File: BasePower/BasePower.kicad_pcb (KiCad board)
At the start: 4 copper layers, 80.5 x 40 mm, 59 parts, among them J1 VIN, J2 3.3V, U1 TPS552892, U2 TLVM13640, U3 TPSM33625F

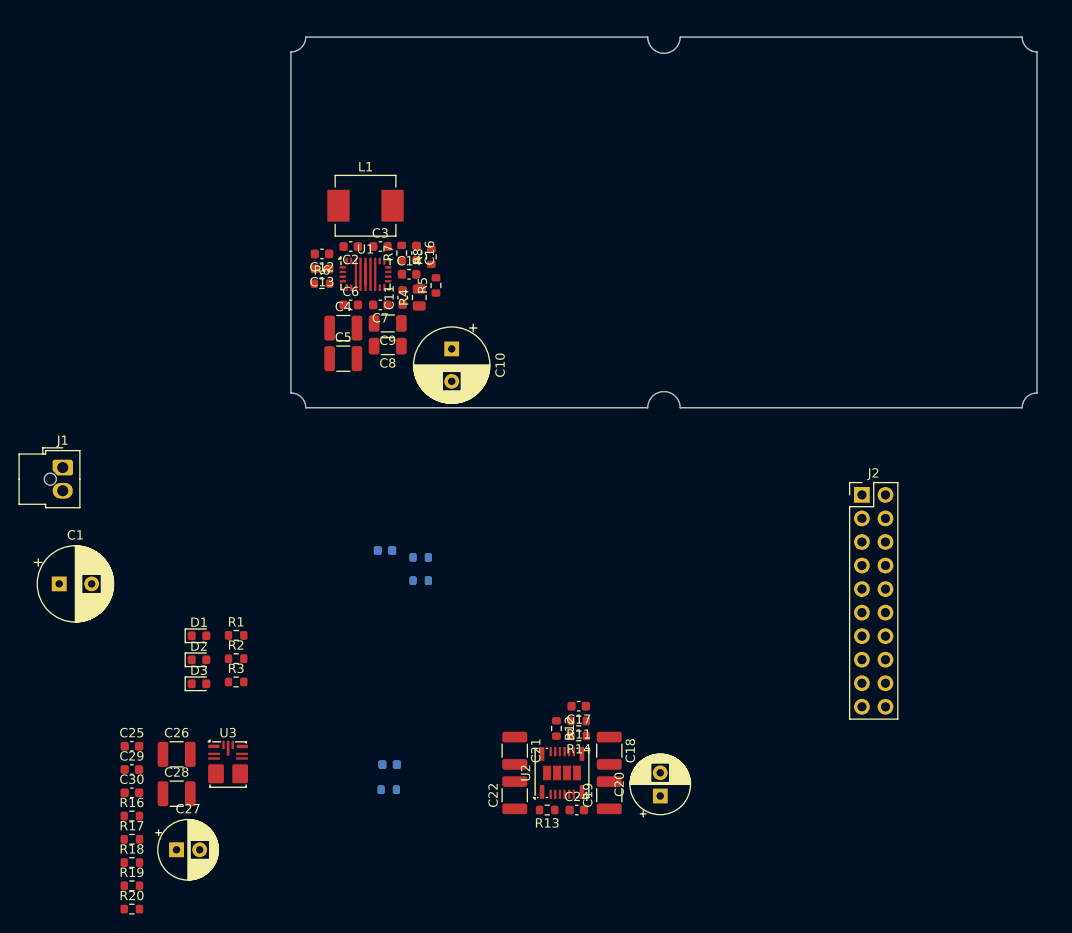
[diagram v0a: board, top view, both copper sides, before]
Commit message: BasePower layout mostly done
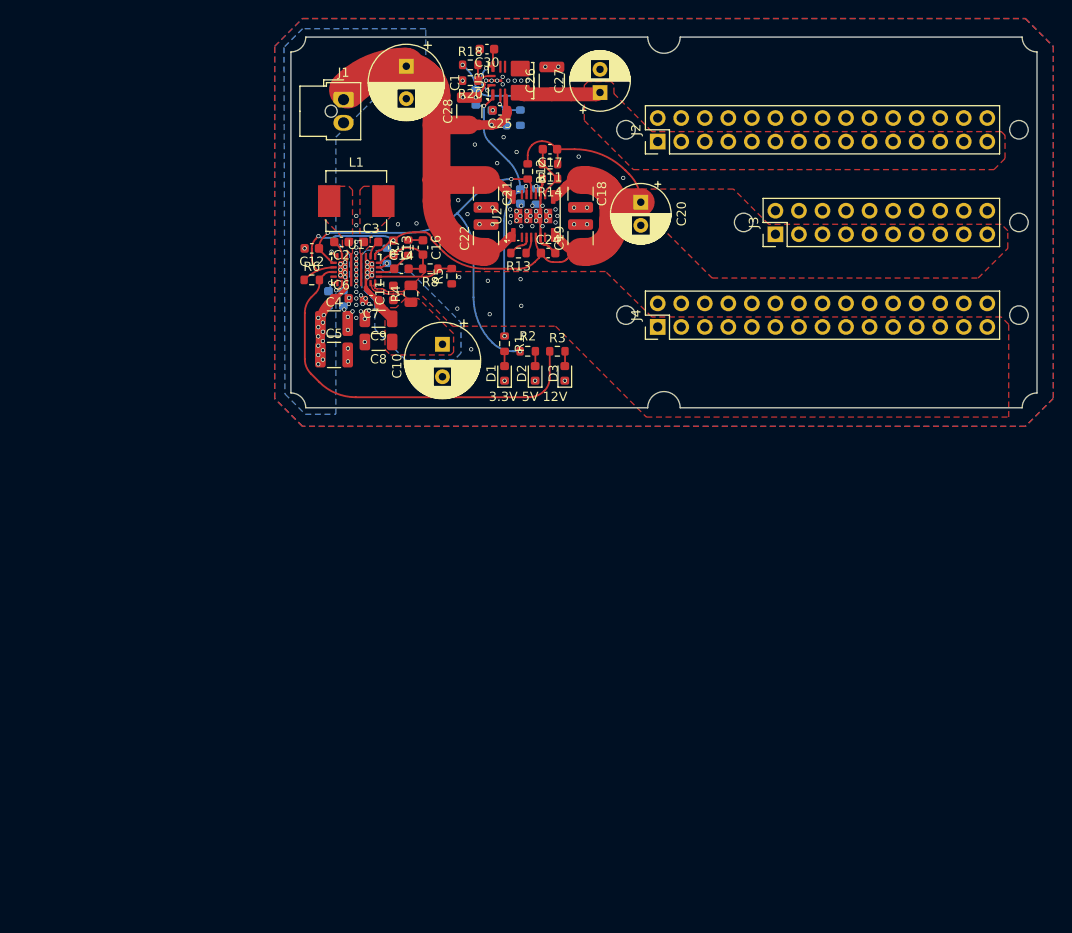
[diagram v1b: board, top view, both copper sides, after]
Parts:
- added Hole1: Hole_2mm, BW_PassiveMechanical:Hole_2mm, F.Cu at (145.9, 90.0)
- added Hole2: Hole_2mm, BW_PassiveMechanical:Hole_2mm, F.Cu at (188.3, 90.0)
- added Hole3: Hole_2mm, BW_PassiveMechanical:Hole_2mm, F.Cu at (158.6, 100.0)
- added Hole4: Hole_2mm, BW_PassiveMechanical:Hole_2mm, F.Cu at (188.3, 100.0)
- added Hole5: Hole_2mm, BW_PassiveMechanical:Hole_2mm, F.Cu at (145.9, 110.0)
- added Hole6: Hole_2mm, BW_PassiveMechanical:Hole_2mm, F.Cu at (188.3, 110.0)
- added J3: 5V, Connector_PinHeader_2.54mm:PinHeader_2x10_P2.54mm_Vertical, F.Cu at (162.0, 101.3)
- added J4: 12V, Connector_PinHeader_2.54mm:PinHeader_2x15_P2.54mm_Vertical, F.Cu at (149.3, 111.3)
- C29, R16, R17, R19: moved to B.Cu
- J2: footprint Connector_PinHeader_2.54mm:PinHeader_2x10_P2.54mm_Vertical -> Connector_PinHeader_2.54mm:PinHeader_2x15_P2.54mm_Vertical
- moved R20 96.6 mm to (129.1, 84.7), turned to 180 degrees
- moved C27 93.6 mm to (143.1, 86.0), turned to 90 degrees
- moved R18 93.5 mm to (129.1, 83.0)
- moved R19 92.9 mm to (134.5, 88.7), turned to -90 degrees
- moved C30 88.9 mm to (130.9, 81.3), turned to 180 degrees
- moved R17 88.2 mm to (129.7, 86.5), turned to -90 degrees
- moved R16 84.4 mm to (132.2, 89.5)
- moved C26 83.2 mm to (137.9, 84.7), turned to 90 degrees
- moved C29 81.4 mm to (132.2, 87.9), turned to 180 degrees
- moved C28 80.1 mm to (129.0, 88.0), turned to 90 degrees
- moved U3 79.9 mm to (133.5, 84.7), turned to 90 degrees
- moved C25 79.3 mm to (132.3, 87.9), turned to 180 degrees
- moved C1 67.2 mm to (122.2, 83.1), turned to -90 degrees
- moved R15 65.9 mm to (136.2, 97.2), turned to -90 degrees
- moved C20 64.1 mm to (147.5, 97.8), turned to -90 degrees
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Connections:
- J2 pad 1: GND -> /3.3V Buck/3.3V
- J2 pad 10: /3.3V Buck/3.3V -> GND
- J2 pad 11: GND -> /3.3V Buck/3.3V
- J2 pad 12: /3.3V Buck/3.3V -> GND
- J2 pad 13: GND -> /3.3V Buck/3.3V
- J2 pad 14: /3.3V Buck/3.3V -> GND
- J2 pad 15: GND -> /3.3V Buck/3.3V
- J2 pad 16: /3.3V Buck/3.3V -> GND
- J2 pad 17: GND -> /3.3V Buck/3.3V
- J2 pad 18: /3.3V Buck/3.3V -> GND
- J2 pad 19: GND -> /3.3V Buck/3.3V
- J2 pad 2: /3.3V Buck/3.3V -> GND
- J2 pad 20: /3.3V Buck/3.3V -> GND
- J2 pad 3: GND -> /3.3V Buck/3.3V
- J2 pad 4: /3.3V Buck/3.3V -> GND
- J2 pad 5: GND -> /3.3V Buck/3.3V
- J2 pad 6: /3.3V Buck/3.3V -> GND
- J2 pad 7: GND -> /3.3V Buck/3.3V
- J2 pad 8: /3.3V Buck/3.3V -> GND
- J2 pad 9: GND -> /3.3V Buck/3.3V
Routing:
- net /12V Buck-Boost/5V: track 0.00 -> 85.0 mm, vias 0 -> 2
- net /12V Buck-Boost/VIN: track 0.00 -> 66.0 mm, vias 0 -> 20
- net /5V Buck/5VPG: track 0.00 -> 47.5 mm, vias 0 -> 3
- net /12V Buck-Boost/PG: track 0.00 -> 43.2 mm
- net /3.3V Buck/PG: track 0.00 -> 30.8 mm, vias 0 -> 3
- net /3.3V Buck/3.3V: track 0.00 -> 25.5 mm, vias 0 -> 1
- net GND: track 0.00 -> 22.1 mm, vias 0 -> 104
- net Net-(U1-ISP): track 0.00 -> 12.4 mm, vias 0 -> 7
- net Net-(U1-FB): track 0.00 -> 8.22 mm
- net Net-(U3-RT/MODE/SYNC): track 0.00 -> 6.24 mm, vias 0 -> 2
- net Net-(U2-FB): track 0.00 -> 6.14 mm
- net /12V Buck-Boost/12V: track 0.00 -> 5.45 mm
- net Net-(U3-EN): track 0.00 -> 5.18 mm, vias 0 -> 1
- net Net-(U1-COMP): track 0.00 -> 3.83 mm
- net Net-(U3-FB/BIAS): track 0.00 -> 3.29 mm
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- added copper zone on F.Cu, net /12V Buck-Boost/12V
- added copper zone on F.Cu, net /12V Buck-Boost/5V
- added copper zone on B.Cu, net /12V Buck-Boost/VIN
- added copper zone on F.Cu, net /3.3V Buck/3.3V
- added copper zone on B.Cu, net GND
- added copper zone on F.Cu, net GND
- added copper zone on In1.Cu, net GND
- added copper zone on In2.Cu, net GND
- added copper zone on B.Cu, net Net-(U1-ISP)
- added copper zone on F.Cu, net Net-(U1-ISP)
- added copper zone on F.Cu, net Net-(U1-SW1)
- added copper zone on F.Cu, net Net-(U1-SW2)
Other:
- board text added: "3.3V 5V 12V"

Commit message: BasePower design and inventory done
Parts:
- added C2: ?pF, Capacitor_SMD:C_0603_1608Metric, F.Cu at (111.5, 98.5)
- added C3: ?pF, Capacitor_SMD:C_0603_1608Metric, F.Cu at (122.1, 98.5)
- added R4: ?Ω, Resistor_SMD:R_1206_3216Metric, F.Cu at (111.1, 94.6)
- added R5: ?Ω, Resistor_SMD:R_1206_3216Metric, F.Cu at (122.5, 94.6)
- added R6: 50Ω, Resistor_SMD:R_0603_1608Metric, B.Cu at (116.0, 97.1)
- added R7: 50Ω, Resistor_SMD:R_0603_1608Metric, B.Cu at (122.2, 95.0)
- added REF**: BW_Logo_7.5x4.8mm, BW_Logo:BW_Logo_7.5x4.8mm, F.Cu at (182.1, 83.6)
- added TP1: SW1, Connector_Coaxial:U.FL_Molex_MCRF_73412-0110_Vertical, B.Cu at (116.8, 93.7)
- added TP2: SW2, Connector_Coaxial:U.FL_Molex_MCRF_73412-0110_Vertical, B.Cu at (123.2, 98.4)
- renumbered C8 to C10, C9 to C11, C10 to C12, C11 to C13, C12 to C14, C13 to C15, C14 to C16, C15 to C17, C16 to C18, C17 to C19, C18 to C20, C19 to C21, C20 to C22, C21 to C23, C22 to C24, C23 to C25, C24 to C26, C25 to C27, C26 to C28, C27 to C29, C28 to C30, C29 to C31, C30 to C32, C2 to C4, C3 to C5, C4 to C6, C5 to C7, C6 to C8, C7 to C9, R6 to R10, R7 to R11, R8 to R12, R9 to R13, R10 to R14, R11 to R15, R12 to R16, R13 to R17, R14 to R18, R15 to R19, R16 to R20, R17 to R21, R18 to R22, R19 to R23, R20 to R24, R4 to R8, R5 to R9
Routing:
- net GND: track 22.1 -> 35.4 mm, vias 104 -> 108
- net Net-(U1-SW2): track 0.00 -> 5.01 mm, vias 0 -> 1
- net Net-(U1-SW1): track 0.00 -> 3.08 mm, vias 0 -> 1
- net Net-(TP2-In): track 0.00 -> 1.94 mm
- net Net-(TP1-In): track 0.00 -> 1.91 mm
- net Net-(C2-Pad1): track 0.00 -> 1.76 mm
- net Net-(C3-Pad1): track 0.00 -> 1.76 mm
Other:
- board text added: "+ -"
- board text added: "12V"
- board text added: "3.3V"
- board text added: "5V"
- board text added: "Modular Audio Base Power"
- board text added: "Power Good"

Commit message: BasePower v1.1: Now with fuses
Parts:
- added F1: 2.5A, Fuse:Fuse_0603_1608Metric, F.Cu at (145.9, 92.8)
- added F2: 4A, Fuse:Fuse_0603_1608Metric, F.Cu at (152.5, 97.8)
- added F3: 5A, Fuse:Fuse_0603_1608Metric, F.Cu at (127.8, 108.2)
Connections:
- J2 pad 1: /3.3V Buck/3.3V -> Net-(J2-Pin_1)
- J2 pad 11: /3.3V Buck/3.3V -> Net-(J2-Pin_1)
- J2 pad 13: /3.3V Buck/3.3V -> Net-(J2-Pin_1)
- J2 pad 15: /3.3V Buck/3.3V -> Net-(J2-Pin_1)
- J2 pad 17: /3.3V Buck/3.3V -> Net-(J2-Pin_1)
- J2 pad 19: /3.3V Buck/3.3V -> Net-(J2-Pin_1)
- J2 pad 21: /3.3V Buck/3.3V -> Net-(J2-Pin_1)
- J2 pad 23: /3.3V Buck/3.3V -> Net-(J2-Pin_1)
- J2 pad 25: /3.3V Buck/3.3V -> Net-(J2-Pin_1)
- J2 pad 27: /3.3V Buck/3.3V -> Net-(J2-Pin_1)
- J2 pad 29: /3.3V Buck/3.3V -> Net-(J2-Pin_1)
- J2 pad 3: /3.3V Buck/3.3V -> Net-(J2-Pin_1)
- J2 pad 5: /3.3V Buck/3.3V -> Net-(J2-Pin_1)
- J2 pad 7: /3.3V Buck/3.3V -> Net-(J2-Pin_1)
- J2 pad 9: /3.3V Buck/3.3V -> Net-(J2-Pin_1)
- J3 pad 1: /12V Buck-Boost/5V -> Net-(J3-Pin_1)
- J3 pad 11: /12V Buck-Boost/5V -> Net-(J3-Pin_1)
- J3 pad 13: /12V Buck-Boost/5V -> Net-(J3-Pin_1)
- J3 pad 15: /12V Buck-Boost/5V -> Net-(J3-Pin_1)
- J3 pad 17: /12V Buck-Boost/5V -> Net-(J3-Pin_1)
- J3 pad 19: /12V Buck-Boost/5V -> Net-(J3-Pin_1)
- J3 pad 3: /12V Buck-Boost/5V -> Net-(J3-Pin_1)
- J3 pad 5: /12V Buck-Boost/5V -> Net-(J3-Pin_1)
- J3 pad 7: /12V Buck-Boost/5V -> Net-(J3-Pin_1)
- J3 pad 9: /12V Buck-Boost/5V -> Net-(J3-Pin_1)
- J4 pad 1: /12V Buck-Boost/12V -> Net-(J4-Pin_1)
- J4 pad 11: /12V Buck-Boost/12V -> Net-(J4-Pin_1)
- J4 pad 13: /12V Buck-Boost/12V -> Net-(J4-Pin_1)
- J4 pad 15: /12V Buck-Boost/12V -> Net-(J4-Pin_1)
- J4 pad 17: /12V Buck-Boost/12V -> Net-(J4-Pin_1)
- J4 pad 19: /12V Buck-Boost/12V -> Net-(J4-Pin_1)
- J4 pad 21: /12V Buck-Boost/12V -> Net-(J4-Pin_1)
- J4 pad 23: /12V Buck-Boost/12V -> Net-(J4-Pin_1)
- J4 pad 25: /12V Buck-Boost/12V -> Net-(J4-Pin_1)
- J4 pad 27: /12V Buck-Boost/12V -> Net-(J4-Pin_1)
- J4 pad 29: /12V Buck-Boost/12V -> Net-(J4-Pin_1)
- J4 pad 3: /12V Buck-Boost/12V -> Net-(J4-Pin_1)
- J4 pad 5: /12V Buck-Boost/12V -> Net-(J4-Pin_1)
- J4 pad 7: /12V Buck-Boost/12V -> Net-(J4-Pin_1)
- J4 pad 9: /12V Buck-Boost/12V -> Net-(J4-Pin_1)
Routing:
- net /3.3V Buck/3.3V: track 25.5 -> 32.4 mm
- net /12V Buck-Boost/5V: track 85.0 -> 89.3 mm
- added copper zone on F.Cu, net Net-(J2-Pin_1)
- added copper zone on F.Cu, net Net-(J3-Pin_1)
- added copper zone on F.Cu, net Net-(J4-Pin_1)
- removed copper zone on F.Cu, net /12V Buck-Boost/5V
- removed copper zone on F.Cu, net /3.3V Buck/3.3V
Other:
- board text added: "2.5A max"
- board text added: "4A max"
- board text added: "5A max"
- board text added: "Modular Audio Base Power v1.1"
- board text removed: "Modular Audio Base Power"

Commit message: BasePower v1.2 + inventory
Added 12V clean LDO and improved power good display
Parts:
- removed the R10 at (112.0, 106.2)
- removed the R16 at (135.3, 94.5)
- removed the R21 at (129.7, 86.5)
- added C33: 10µF 50V, Capacitor_SMD:C_1206_3216Metric, B.Cu at (141.8, 107.5)
- added C34: 0.1µF, Capacitor_SMD:C_0603_1608Metric, B.Cu at (141.0, 109.4)
- added C35: 22µF 16V, Capacitor_SMD:C_1210_3225Metric, B.Cu at (141.8, 112.3)
- added C36: 470µF 16V, Capacitor_THT:CP_Radial_D6.3mm_P2.50mm, F.Cu at (158.9, 116.5)
- added C37: 1µF 50Vl, Capacitor_SMD:C_0805_2012Metric, B.Cu at (136.1, 106.1)
- added D4: Green, LED_SMD:LED_0603_1608Metric, F.Cu at (141.6, 116.3)
- added JP1: 0.8V, Jumper:SolderJumper-2_P1.3mm_Open_RoundedPad1.0x1.5mm, B.Cu at (131.4, 113.6)
- added JP2: 0.2V, Jumper:SolderJumper-2_P1.3mm_Open_RoundedPad1.0x1.5mm, B.Cu at (131.4, 108.4)
- added JP3: 0.4V, Jumper:SolderJumper-2_P1.3mm_Open_RoundedPad1.0x1.5mm, B.Cu at (131.4, 111.0)
- added JP4: 0.1V, Jumper:SolderJumper-2_P1.3mm_Open_RoundedPad1.0x1.5mm, B.Cu at (132.6, 105.8)
- added Q1: NX138BK, Package_TO_SOT_SMD:SOT-23, B.Cu at (138.6, 117.6)
- added Q2: NX138BK, Package_TO_SOT_SMD:SOT-23, B.Cu at (142.6, 117.6)
- added R1: 1kΩ, Resistor_SMD:R_0603_1608Metric, B.Cu at (132.4, 91.8)
- added R3: 3.3kΩ, Resistor_SMD:R_0603_1608Metric, F.Cu at (135.3, 94.3)
- added R5: 2kΩ, Resistor_SMD:R_0603_1608Metric, F.Cu at (111.6, 105.2)
- added R7: 1kΩ, Resistor_SMD:R_0603_1608Metric, F.Cu at (140.1, 114.8)
- added R8: 4.7kΩ, Resistor_SMD:R_0603_1608Metric, B.Cu at (146.9, 115.8)
- added R9: 1kΩ, Resistor_SMD:R_0603_1608Metric, B.Cu at (145.3, 117.6)
- added U4: TPS7A47, Package_DFN_QFN:Texas_RGW0020A_VQFN-20-1EP_5x5mm_P0.65mm_EP3.15x3.15mm, B.Cu at (136.3, 110.4)
- R2: renamed from R1; value ?kΩ -> 0Ω
- R4: renamed from R2; value ?kΩ -> 0Ω
- R6: renamed from R3; value ?kΩ -> 1kΩ
- moved D1 0.80 mm to (132.0, 116.3)
- moved D3 0.80 mm to (138.5, 116.3)
- moved R2 0.80 mm to (132.0, 113.1)
- moved R4 0.80 mm to (134.5, 113.9)
- moved R6 0.80 mm to (137.7, 113.9)
- moved D2 0.80 mm to (135.3, 116.3)
- moved TP2 0.10 mm to (123.2, 98.3)
- renumbered R4 to R10, R5 to R11, R6 to R12, R7 to R13, R8 to R14, R9 to R15, R11 to R16, R12 to R17, R13 to R18, R14 to R19, R15 to R20, R17 to R21, R18 to R22, R19 to R23, R20 to R24, R22 to R25, R23 to R26, R24 to R27
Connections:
- net /5V Buck/5VPG renamed /12V Buck-Boost/EN
- D3 pad 1: GND -> Net-(D3-K)
- F3 pad 2: Net-(J4-Pin_1) -> /12V Clean LDO/12V
- J4 pad 1: Net-(J4-Pin_1) -> /12V Clean LDO/12V
- J4 pad 11: Net-(J4-Pin_1) -> /12V Clean LDO/12V
- J4 pad 13: Net-(J4-Pin_1) -> /12V Clean LDO/12V
- J4 pad 15: Net-(J4-Pin_1) -> /12V Clean LDO/12V
- J4 pad 17: Net-(J4-Pin_1) -> /12V Clean LDO/12V
- J4 pad 19: Net-(J4-Pin_1) -> /12V Clean LDO/12V
- J4 pad 21: Net-(J4-Pin_1) -> /12V Clean LDO/12V
- J4 pad 23: Net-(J4-Pin_1) -> /12V Clean LDO/12V
- J4 pad 25: Net-(J4-Pin_1) -> /12V Clean LDO/12VC
- J4 pad 27: Net-(J4-Pin_1) -> /12V Clean LDO/12VC
- J4 pad 29: Net-(J4-Pin_1) -> /12V Clean LDO/12VC
- J4 pad 3: Net-(J4-Pin_1) -> /12V Clean LDO/12V
- J4 pad 5: Net-(J4-Pin_1) -> /12V Clean LDO/12V
- J4 pad 7: Net-(J4-Pin_1) -> /12V Clean LDO/12V
- J4 pad 9: Net-(J4-Pin_1) -> /12V Clean LDO/12V
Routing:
- net /12V Clean LDO/12VC: track 0.00 -> 79.1 mm
- net Net-(J3-Pin_1): track 0.00 -> 50.9 mm, vias 0 -> 2
- net Net-(J2-Pin_1): track 0.00 -> 14.3 mm, vias 0 -> 1
- net /12V Clean LDO/12V: track 0.00 -> 13.3 mm, vias 0 -> 4
- net GND: track 35.4 -> 48.0 mm, vias 108 -> 122
- net /12V Buck-Boost/5V: track 89.3 -> 78.6 mm
- net Net-(JP1-B): track 0.00 -> 4.72 mm
- net /12V Buck-Boost/PG: track 43.2 -> 47.0 mm
- net Net-(JP4-B): track 0.00 -> 3.66 mm
- net Net-(Q2-G): track 0.00 -> 3.43 mm
- net Net-(JP2-B): track 0.00 -> 3.04 mm
- net Net-(JP3-B): track 0.00 -> 2.90 mm
- net /12V Buck-Boost/EN: track 47.5 -> 49.9 mm
- net Net-(U4-NR): track 0.00 -> 1.96 mm
- net /3.3V Buck/PG: track 30.8 -> 32.4 mm
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- added copper zone on F.Cu, net /12V Clean LDO/12V
- removed copper zone on F.Cu, net Net-(J4-Pin_1)
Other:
- board text added: "11V +0.1V +0.2V +0.4V +0.8V"
- board text added: "12V Clean"
- board text added: "1A max"
- board text added: "3.3V 5V 12V 12C"
- board text added: "5A max incl. clean"
- board text added: "Modular Audio Base Power v1.2"
- board text removed: "3.3V 5V 12V"
- board text removed: "5A max"
- board text removed: "Modular Audio Base Power v1.1"

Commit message: BasePower adjusted LED resistors for equal brightness
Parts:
- R6: value 1kΩ -> 510Ω
- R7: value 1kΩ -> 2.2kΩ
